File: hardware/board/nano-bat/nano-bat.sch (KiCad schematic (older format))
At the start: 14 parts

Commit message: Adding larger microcontroller
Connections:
- wire segments 41 -> 45
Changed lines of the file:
@@
 encoding utf-8
 Sheet 1 6
-Title ""
+Title "NanoBat"
 Date ""
-Rev ""
-Comp ""
-Comment1 ""
+Rev "0.1.0"
+Comp "Vertigo Designs"
+Comment1 "Author: Ryan Summers"
 Comment2 ""
 Comment3 ""
@@
 F2 "Vin" I L 2750 1950 50
 F3 "Vsoc" I R 4000 2050 50
-F4 "Pgood" I R 4000 2700 50
-F5 "Enable" I L 2750 2100 50
-F6 "Vadj" I R 4000 2600 50
+F4 "Pgood" I R 4000 2800 50
+F5 "Vadj" I R 4000 2650 50
 $EndSheet
 $Sheet
@@
 F2 "USB_DP" I L 4550 3950 50
 F3 "USB_DM" I L 4550 4050 50
-F4 "Vadj" I L 4550 2600 50
+F4 "Vadj" I L 4550 2650 50
 F5 "LCD-TFT_DB" I R 6350 5100 50
 F6 "LCD_RS" I R 6350 5200 50
@@
 F21 "TFT_RGB_VSYNC" I R 6350 4600 50
 F22 "TFT_RST" I R 6350 4000 50
-F23 "Vsoc" I L 4550 2700 50
+F23 "Vsoc" I L 4550 2500 50
 F24 "Pgood" I L 4550 2800 50
 $EndSheet
 Wire Wire Line
-	4000 2600 4550 2600
+	4000 2650 4550 2650
 Wire Wire Line
 	2250 1950 2750 1950
@@
 	6350 2800 6950 2800
 Wire Wire Line
-	4000 2050 5000 2050
+	4000 2050 4250 2050
 Wire Wire Line
 	5150 1800 6950 1800
@@
 Wire Wire Line
 	8400 1800 9300 1800
+Wire Wire Line
+	4550 2500 4250 2500
+Wire Wire Line
+	4250 2500 4250 2050
+Connection ~ 4250 2050
+Wire Wire Line
+	4250 2050 5000 2050
+Wire Wire Line
+	4550 2800 4000 2800
 $EndSCHEMATC

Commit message: Adding WIP before reverting
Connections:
- wire segments 45 -> 47
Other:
- moved on the sheet: F?, FB?, J?
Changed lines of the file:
@@
 $Descr A4 11693 8268
 encoding utf-8
-Sheet 1 6
+Sheet 1 5
 Title "NanoBat"
 Date ""
@@
 $EndDescr
 $Sheet
-S 2750 1850 1250 1400
+S 2750 1850 1250 1100
 U 5DD44E3C
 F0 "Power" 50
@@
 F5 "Vadj" I R 4000 2650 50
 $EndSheet
-$Sheet
-S 6950 1450 1450 1550
-U 5DDB3EB5
-F0 "Coulomb Counter" 50
-F1 "coulomb-counter.sch" 50
-F2 "Vbatt_source" I L 6950 1800 50
-F3 "Vbatt_out" I R 8400 1800 50
-F4 "~INT" I L 6950 2600 50
-F5 "~SHDN" I L 6950 2700 50
-F6 "POL" I L 6950 2800 50
-$EndSheet
 $Comp
 L Connector:Screw_Terminal_01x02 J?
 U 1 1 5DDB6C89
-P 9500 1800
-F 0 "J?" H 9580 1792 50  0000 L CNN
-F 1 "Screw_Terminal_01x02" H 9580 1701 50  0000 L CNN
-F 2 "" H 9500 1800 50  0001 C CNN
-F 3 "~" H 9500 1800 50  0001 C CNN
-	1    9500 1800
+P 9200 1800
+F 0 "J?" H 9280 1792 50  0000 L CNN
+F 1 "Screw_Terminal_01x02" H 9280 1701 50  0000 L CNN
+F 2 "" H 9200 1800 50  0001 C CNN
+F 3 "~" H 9200 1800 50  0001 C CNN
+	1    9200 1800
 	1    0    0    -1
 $EndComp
@@
 $EndComp
 $Sheet
-S 6950 3400 1000 1300
+S 6950 3400 1150 1300
 U 5DDBB7A5
 F0 "(Opt) TFT Display" 50
 F1 "tft-display.sch" 50
-$EndSheet
-$Sheet
-S 6950 4950 1000 1150
-U 5DDBB9AB
-F0 "(Opt) LCD Character Display" 50
-F1 "lcd-display.sch" 50
+F2 "BL_CNTRL" I L 6950 4100 50
+F3 "SDO" I L 6950 3700 50
+F4 "SDI" I L 6950 3800 50
+F5 "~CS" I L 6950 3500 50
+F6 "SCL" I L 6950 3600 50
+F7 "RESET" I L 6950 4250 50
+F8 "D~CX" I L 6950 4000 50
 $EndSheet
 $Comp
@@
 L Device:Polyfuse F?
 U 1 1 5DDC9FB5
-P 3700 3750
-F 0 "F?" V 3475 3750 50  0000 C CNN
-F 1 "Polyfuse" V 3600 3700 50  0000 C CNN
-F 2 "" H 3750 3550 50  0001 L CNN
-F 3 "~" H 3700 3750 50  0001 C CNN
-	1    3700 3750
+P 3450 3750
+F 0 "F?" V 3225 3750 50  0000 C CNN
+F 1 "Polyfuse" V 3350 3700 50  0000 C CNN
+F 2 "" H 3500 3550 50  0001 L CNN
+F 3 "~" H 3450 3750 50  0001 C CNN
+	1    3450 3750
 	0    1    1    0
 $EndComp
@@
 L Device:Ferrite_Bead_Small FB?
 U 1 1 5DDCAA04
-P 3400 3750
-F 0 "FB?" V 3163 3750 50  0000 C CNN
-F 1 "Ferrite_Bead_Small" V 3500 3750 50  0001 C CNN
-F 2 "" V 3330 3750 50  0001 C CNN
-F 3 "~" H 3400 3750 50  0001 C CNN
-	1    3400 3750
+P 3750 3750
+F 0 "FB?" V 3600 3750 50  0000 C CNN
+F 1 "Ferrite_Bead_Small" V 3850 3750 50  0001 C CNN
+F 2 "" V 3680 3750 50  0001 C CNN
+F 3 "~" H 3750 3750 50  0001 C CNN
+	1    3750 3750
 	0    1    1    0
 $EndComp
@@
 Wire Wire Line
 	3300 3750 3250 3750
-Wire Wire Line
-	3550 3750 3500 3750
 Wire Wire Line
 	2850 4400 2850 4350
@@
 L power:GND #PWR?
 U 1 1 5DDEEF41
-P 9250 2000
-F 0 "#PWR?" H 9250 1750 50  0001 C CNN
-F 1 "GND" H 9255 1827 50  0000 C CNN
-F 2 "" H 9250 2000 50  0001 C CNN
-F 3 "" H 9250 2000 50  0001 C CNN
-	1    9250 2000
-	1    0    0    -1
-$EndComp
-Wire Wire Line
-	9250 2000 9250 1900
-Wire Wire Line
-	9250 1900 9300 1900
+P 8950 2000
+F 0 "#PWR?" H 8950 1750 50  0001 C CNN
+F 1 "GND" H 8955 1827 50  0000 C CNN
+F 2 "" H 8950 2000 50  0001 C CNN
+F 3 "" H 8950 2000 50  0001 C CNN
+	1    8950 2000
+	1    0    0    -1
+$EndComp
+Wire Wire Line
+	8950 2000 8950 1900
+Wire Wire Line
+	8950 1900 9000 1900
 $Comp
 L Connector_Generic:Conn_01x02 J?
@@
 Wire Wire Line
 	2800 4650 2800 4600
+Wire Wire Line
+	4000 2650 4550 2650
+Wire Wire Line
+	2250 1950 2750 1950
+Wire Wire Line
+	4000 2050 4250 2050
+Wire Wire Line
+	5150 1800 6950 1800
+Wire Wire Line
+	1050 1300 5000 1300
+Wire Wire Line
+	5000 1300 5000 1550
+Wire Wire Line
+	3250 3950 4550 3950
+Wire Wire Line
+	3250 4050 4550 4050
+Text Notes 8650 2300 0    50   ~ 0
+TODO: Add optional JST connector here
+Wire Wire Line
+	4550 2500 4250 2500
+Wire Wire Line
+	4250 2500 4250 2050
+Connection ~ 4250 2050
+Wire Wire Line
+	4250 2050 5000 2050
+Wire Wire Line
+	4550 2800 4000 2800
 $Sheet
-S 4550 2400 1800 3700
+S 4550 2400 1800 2300
 U 5DDB3E1D
 F0 "Microcontroller" 50
@@
 F3 "USB_DM" I L 4550 4050 50
 F4 "Vadj" I L 4550 2650 50
-F5 "LCD-TFT_DB" I R 6350 5100 50
-F6 "LCD_RS" I R 6350 5200 50
-F7 "LCD_R~W" I R 6350 5300 50
-F8 "LCD_EN" I R 6350 5400 50
-F9 "CC_~INT" I R 6350 2600 50
-F10 "CC_POL" I R 6350 2800 50
-F11 "CC_~SHDN" I R 6350 2700 50
-F12 "TFT_SCK" I R 6350 3550 50
-F13 "TFT_MISO" I R 6350 3650 50
-F14 "TFT_MOSI" I R 6350 3750 50
-F15 "TFT_~CS" I R 6350 3850 50
-F16 "TFT_RD" I R 6350 4100 50
-F17 "TFT_WR" I R 6350 4200 50
-F18 "TFT_RGB_EN" I R 6350 4300 50
-F19 "TFT_RGB_DOTCLK" I R 6350 4400 50
-F20 "TFT_RGB_HSYNC" I R 6350 4500 50
-F21 "TFT_RGB_VSYNC" I R 6350 4600 50
-F22 "TFT_RST" I R 6350 4000 50
-F23 "Vsoc" I L 4550 2500 50
-F24 "Pgood" I L 4550 2800 50
+F5 "TFT_SCK" I R 6350 3600 50
+F6 "TFT_MISO" I R 6350 3700 50
+F7 "TFT_MOSI" I R 6350 3800 50
+F8 "TFT_~CS" I R 6350 3500 50
+F9 "TFT_RST" I R 6350 4250 50
+F10 "Vsoc" I L 4550 2500 50
+F11 "Pgood" I L 4550 2800 50
 $EndSheet
 Wire Wire Line
-	4000 2650 4550 2650
-Wire Wire Line
-	2250 1950 2750 1950
-Wire Wire Line
-	6350 2600 6950 2600
-Wire Wire Line
-	6350 2700 6950 2700
-Wire Wire Line
-	6350 2800 6950 2800
-Wire Wire Line
-	4000 2050 4250 2050
-Wire Wire Line
-	5150 1800 6950 1800
-Wire Wire Line
-	1050 1300 5000 1300
-Wire Wire Line
-	5000 1300 5000 1550
-Wire Wire Line
-	3250 3950 4550 3950
-Wire Wire Line
-	3250 4050 4550 4050
-Text Notes 8950 2300 0    50   ~ 0
-TODO: Add optional JST connector here
-Wire Wire Line
-	8400 1800 9300 1800
-Wire Wire Line
-	4550 2500 4250 2500
-Wire Wire Line
-	4250 2500 4250 2050
-Connection ~ 4250 2050
-Wire Wire Line
-	4250 2050 5000 2050
-Wire Wire Line
-	4550 2800 4000 2800
+	8100 1800 9000 1800
+$Sheet
+S 6950 1450 1150 1450
+U 5DDB3EB5
+F0 "Coulomb Counter" 50
+F1 "coulomb-counter.sch" 50
+F2 "Vbatt_source" I L 6950 1800 50
+F3 "Vbatt_out" I R 8100 1800 50
+F4 "~AL~CC" I L 6950 2550 50
+F5 "SCL" I L 6950 2700 50
+F6 "SDA" I L 6950 2800 50
+$EndSheet
+Wire Wire Line
+	6350 3800 6950 3800
+Wire Wire Line
+	6950 3700 6350 3700
+Wire Wire Line
+	6350 3600 6950 3600
+Wire Wire Line
+	6950 3500 6350 3500
+Wire Wire Line
+	6350 4250 6950 4250
+Wire Wire Line
+	3650 3750 3600 3750
 $EndSCHEMATC

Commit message: Adding complete schematic
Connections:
- wire segments 47 -> 52
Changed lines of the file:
@@
 F10 "Vsoc" I L 4550 2500 50
 F11 "Pgood" I L 4550 2800 50
+F12 "TFT_BL_CNTRL" I R 6350 4100 50
+F13 "CC_SDA" I R 6350 2800 50
+F14 "CC_SCL" I R 6350 2700 50
+F15 "CC_~AL~CC" I R 6350 2550 50
+F16 "TFT_D~CX" I R 6350 4000 50
 $EndSheet
 Wire Wire Line
@@
 Wire Wire Line
 	3650 3750 3600 3750
+Wire Wire Line
+	6350 4000 6950 4000
+Wire Wire Line
+	6950 4100 6350 4100
+Wire Wire Line
+	6350 2700 6950 2700
+Wire Wire Line
+	6950 2800 6350 2800
+Wire Wire Line
+	6350 2550 6950 2550
 $EndSCHEMATC

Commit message: Adding first-pass revisions and annotations, part selection
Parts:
- removed F?: Polyfuse, symbol Device:Polyfuse
- removed FB? (x3): Ferrite_Bead_Small, symbol Device:Ferrite_Bead_Small
- removed J?: Conn_01x02, symbol Connector_Generic:Conn_01x02
- removed JP?: Jumper_3_Bridged12, symbol Jumper:Jumper_3_Bridged12
- removed Q?: Q_PMOS_DGS, symbol Device:Q_PMOS_DGS
- added D102: LED, LED_SMD:LED_0805_2012Metric, symbol Device:LED
- added F102: Polyfuse, Fuse:Fuse_1812_4532Metric, symbol Device:Polyfuse
- added FB101, FB102, FB103: Ferrite_Bead_Small, Resistor_SMD:R_0603_1608Metric, symbol Device:Ferrite_Bead_Small
- added J104: Conn_01x02, Connector_JST:JST_PH_S2B-PH-SM4-TB_1x02-1MP_P2.00mm_Horizontal, symbol Connector_Generic:Conn_01x02
- added Q101: Q_PMOS_GSD, Package_TO_SOT_SMD:SOT-23, symbol Device:Q_PMOS_GSD
- added R103: 1k, Resistor_SMD:R_0603_1608Metric, symbol Device:R_US
- D101: renamed from D?; footprint (none) -> Diode_SMD:D_SMA; symbol Device:D -> Device:D_Schottky_Small_ALT; Part (none) -> 641-1015-1-ND
- F101: renamed from F?; footprint (none) -> Fuse:Fuse_1812_4532Metric; Part (none) -> 507-1763-1-ND
- J101: renamed from J?; footprint (none) -> footprints:CUI_PJ-202B
- J102: renamed from J?; footprint (none) -> footprints:USB-MICRO-B-HIROSE-UX60-MB-5S8; Part (none) -> H2960CT-ND
- J103: renamed from J?; footprint (none) -> TerminalBlock_Phoenix:TerminalBlock_Phoenix_PT-1,5-2-3.5-H_1x02_P3.50mm_Horizontal; Part (none) -> 277-1721-ND
- R101: renamed from R?; footprint (none) -> Resistor_SMD:R_0603_1608Metric; Part (none) -> 311-1.0KGRCT-ND
- R102: renamed from R?; footprint (none) -> Resistor_SMD:R_0603_1608Metric; Part (none) -> RR08P100KDCT-ND
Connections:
- wire segments 52 -> 60
- no-connect marks 1 -> 2
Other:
- note removed: "TODO: Add optional JST connector here"
- moved on the sheet: F101, J101, J102, J103, R101, R102

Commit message: Adding 3D models, reorg, minor schematic fixes
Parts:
- J101: Part (none) -> CP-202B-ND
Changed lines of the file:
@@
 F 2 "footprints:CUI_PJ-202B" H 1450 2660 50  0001 C CNN
 F 3 "~" H 1450 2660 50  0001 C CNN
+F 4 "CP-202B-ND" H 1400 2700 50  0001 C CNN "Part"
 	1    1400 2700
 	1    0    0    -1

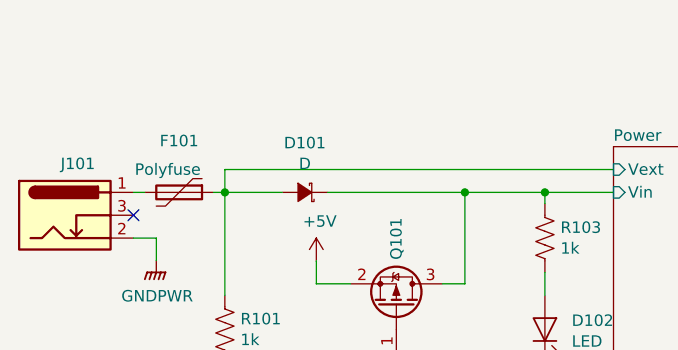
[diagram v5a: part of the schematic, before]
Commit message: Adding docs to schematic
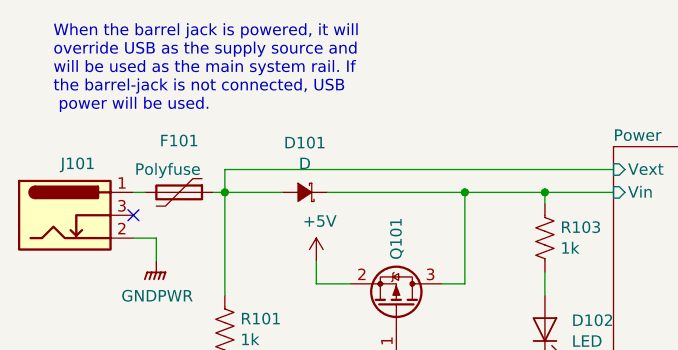
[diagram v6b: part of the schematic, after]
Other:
- note added: "When the barrel jack is powered, it will \noverride USB as the supply source and \nwill be used as the main system rail. If \nthe barrel-jack is not connected, USB\n power will be used."
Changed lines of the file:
@@
 	1    0    0    -1
 $EndComp
+Text Notes 1350 2250 0    50   ~ 0
+When the barrel jack is powered, it will \noverride USB as the supply source and \nwill be used as the main system rail. If \nthe barrel-jack is not connected, USB\n power will be used.
 $EndSCHEMATC

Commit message: Adding 0.1.0 of board spin
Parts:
- removed D101: D, Diode_SMD:D_SMA, symbol Device:D_Schottky_Small_ALT
- removed FB101, FB102: Ferrite_Bead_Small, Resistor_SMD:R_0603_1608Metric, symbol Device:Ferrite_Bead_Small
- removed J102: USB_B_Mini, footprints:USB-MICRO-B-HIROSE-UX60-MB-5S8, symbol Connector:USB_B_Mini
- added C101: 10n, Capacitor_SMD:C_0603_1608Metric, symbol Device:C
- added C102: 0.1u, Capacitor_SMD:C_0603_1608Metric, symbol Device:C
- added H101, H102, H103, H104: e, MountingHole:MountingHole_2.2mm_M2_Pad, symbol Mechanical:MountingHole_Pad
- added J102: USB_C_Receptacle_USB2.0, Connector_USB:USB_C_Receptacle_GCT_USB4085, symbol Connector:USB_C_Receptacle_USB2.0
- added Q102: Q_PMOS_GSD, Package_TO_SOT_SMD:SOT-23, symbol Device:Q_PMOS_GSD
- added R104, R105: 5.1k, Resistor_SMD:R_0603_1608Metric, symbol Device:R_US
- added U101: USBLC6-2SC6, Package_TO_SOT_SMD:SOT-23-6, symbol Power_Protection:USBLC6-2SC6
- R101: value 1k -> 1M; Part 311-1.0KGRCT-ND -> 311-1.00MHRCT-ND
- R102: value 100k -> 1M; Part RR08P100KDCT-ND -> 311-1.00MHRCT-ND
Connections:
- net GNDPWR is gone; now on net GND: J101.2
- net +5V: now also Q102.3 (D); no longer Q101.2 (S)
- net GND: now also Q101.1 (G), R101.2, C101.2, C102.2, H101.1, H102.1, H103.1, H104.1, J102.A1 (GND), J102.A12 (GND), J102.B1 (GND), J102.B12 (GND), R104.2, R105.2, U101.2 (GND); no longer R102.2
- net Power/Vin: now also Q101.2 (S), R102.1, Q102.2 (S); no longer Q101.3 (D)
- net at F102.2: now also C102.1, J102.A4 (VBUS), J102.A9 (VBUS), J102.B4 (VBUS), J102.B9 (VBUS), U101.5 (VBUS)
- net at J101.3: now also R102.2, Q102.1 (G)
- net Power/Vext: no longer names the net of F101.1
- net Power/Vext: now also Q101.3 (D); no longer R101.1
- new net: J102.A5 (CC1), R104.1
- new net: J102.A6 (D+), J102.B6 (D+), U101.3 (IO2)
- new net: J102.A7 (D-), J102.B7 (D-), U101.1 (IO1)
- new net: J102.B5 (CC2), R105.1
- new net: C101.1, J102.S1 (SHIELD), R101.1
- new net USB_N: U101.6 (IO1)
- new net USB_P: U101.4 (IO2)
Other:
- moved on the sheet: F101, F102, FB103, J101

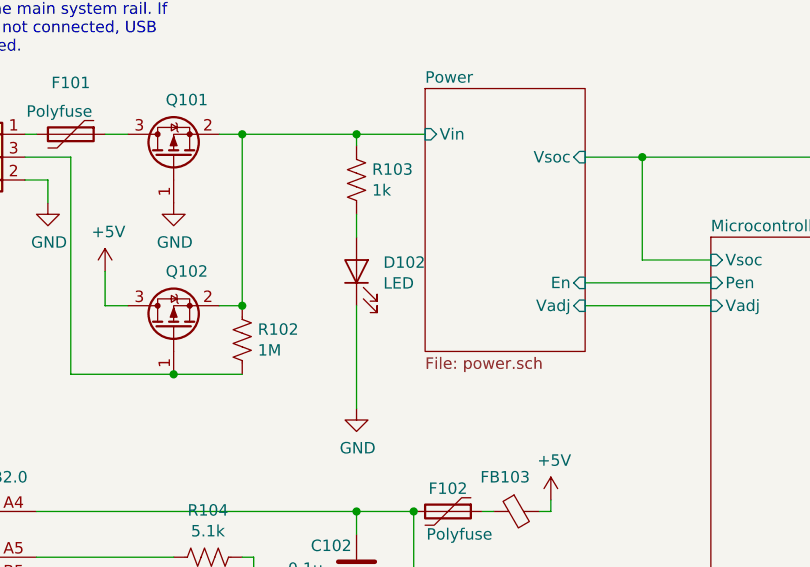
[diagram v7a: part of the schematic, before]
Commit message: Fixing schematic symbol sizes
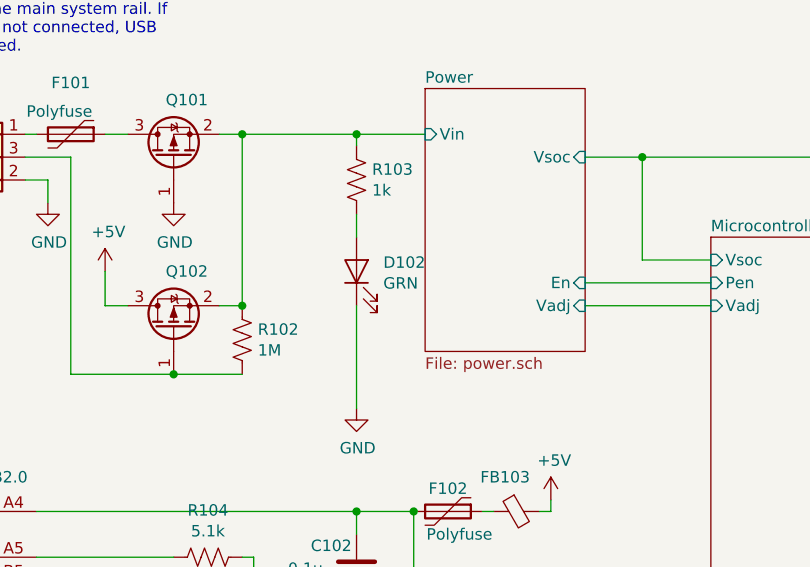
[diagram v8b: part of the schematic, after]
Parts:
- D102: value LED -> GRN
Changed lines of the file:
@@
 AR Path="/5DDD033F" Ref="D102"  Part="1"
 F 0 "D102" V 3539 3083 50  0000 R CNN
-F 1 "LED" V 3448 3083 50  0000 R CNN
+F 1 "GRN" V 3448 3083 50  0000 R CNN
 F 2 "LED_SMD:LED_0805_2012Metric" H 3500 3200 50  0001 C CNN
 F 3 "~" H 3500 3200 50  0001 C CNN
